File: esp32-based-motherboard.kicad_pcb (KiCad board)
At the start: 2 copper layers, 4 parts, among them J1 HR911105A, U1 ESP32-P4_MODULE, U2 LAN8720A, U3 ADM3053

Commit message: Finalized schematics V1
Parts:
- added C1: 470UF, Capacitor_THT:CP_Radial_D6.3mm_P2.50mm, F.Cu at (150.7, 64.6)
- added C10: 0.1uF, Capacitor_SMD:C_0603_1608Metric, F.Cu at (123.8, 72.0)
- added C11: 10uF, Capacitor_SMD:C_0603_1608Metric, F.Cu at (169.9, 105.5)
- added C12: 0.1uF, Capacitor_SMD:C_0603_1608Metric, F.Cu at (169.9, 108.0)
- added C13: 0.1uF, Capacitor_SMD:C_0603_1608Metric, F.Cu at (169.9, 110.5)
- added C14: 0.1uF, Capacitor_SMD:C_0603_1608Metric, F.Cu at (169.9, 113.0)
- added C15: 470pF, Capacitor_SMD:C_0603_1608Metric, F.Cu at (169.9, 115.6)
- added C16: 1uF, Capacitor_SMD:C_0603_1608Metric, F.Cu at (173.9, 105.5)
- added C17: 12pF, Capacitor_SMD:C_0603_1608Metric, F.Cu at (173.9, 108.0)
- added C18: 12pF, Capacitor_SMD:C_0603_1608Metric, F.Cu at (173.9, 110.5)
- added C19: 0.1uF, Capacitor_SMD:C_0603_1608Metric, F.Cu at (123.8, 74.5)
- added C2: 47UF, Capacitor_THT:CP_Radial_D6.3mm_P2.50mm, F.Cu at (150.7, 72.4)
- added C20: 10uF, Capacitor_SMD:C_0603_1608Metric, F.Cu at (123.8, 77.0)
- added C21: 0.01uF, Capacitor_SMD:C_0603_1608Metric, F.Cu at (127.8, 61.9)
- added C22: 0.1uF, Capacitor_SMD:C_0603_1608Metric, F.Cu at (127.8, 64.4)
- added C23: 10uF, Capacitor_SMD:C_0603_1608Metric, F.Cu at (127.8, 66.9)
- added C24: 10nF, Capacitor_SMD:C_0603_1608Metric, F.Cu at (127.8, 69.4)
- added C25: 100nF, Capacitor_SMD:C_0603_1608Metric, F.Cu at (127.8, 72.0)
- added C26: 0.1uF, Capacitor_SMD:C_0603_1608Metric, F.Cu at (127.8, 74.5)
- added C28: 10uF, Capacitor_SMD:C_0603_1608Metric, F.Cu at (127.8, 77.0)
- added C29: 0.1uF, Capacitor_SMD:C_0603_1608Metric, F.Cu at (131.8, 61.9)
- added C3: 10uF, Capacitor_SMD:C_0603_1608Metric, F.Cu at (167.2, 86.6)
- added C30: 0.1uF, Capacitor_SMD:C_0603_1608Metric, F.Cu at (131.8, 64.4)
- added C31: 10uF, Capacitor_SMD:C_0603_1608Metric, F.Cu at (131.8, 66.9)
- added C4: 470UF, Capacitor_THT:CP_Radial_D6.3mm_P2.50mm, F.Cu at (150.7, 80.3)
- added C5: 47UF, Capacitor_THT:CP_Radial_D6.3mm_P2.50mm, F.Cu at (150.7, 88.1)
- added C6: 10uF, Capacitor_SMD:C_0603_1608Metric, F.Cu at (123.8, 61.9)
- added C7: 0.1uF, Capacitor_SMD:C_0603_1608Metric, F.Cu at (123.8, 64.4)
- added C8: 0.1uF, Capacitor_SMD:C_0603_1608Metric, F.Cu at (123.8, 66.9)
- added C9: 10uF, Capacitor_SMD:C_0603_1608Metric, F.Cu at (123.8, 69.4)
- added D1: SS56, Diode_SMD:D_SMB, F.Cu at (173.4, 96.5)
- added D10: SD05C-01F, Diode_SMD:D_SOD-323, F.Cu at (113.7, 113.5)
- added D11: SD05C-01F, Diode_SMD:D_SOD-323, F.Cu at (118.0, 104.7)
- added D12: SD05C-01F, Diode_SMD:D_SOD-323, F.Cu at (118.0, 107.6)
- added D13: SD05C-01F, Diode_SMD:D_SOD-323, F.Cu at (118.0, 110.6)
- added D14: SD05C-01F, Diode_SMD:D_SOD-323, F.Cu at (118.0, 113.5)
- added D15: SD05C-01F, Diode_SMD:D_SOD-323, F.Cu at (122.3, 104.7)
- added D16: LED, LED_SMD:LED_0603_1608Metric, F.Cu at (138.1, 107.8)
- added D17: LED, LED_SMD:LED_0603_1608Metric, F.Cu at (138.1, 110.4)
- added D18: SD05C-01F, Diode_SMD:D_SOD-323, F.Cu at (122.3, 107.6)
- added D19: SD05C-01F, Diode_SMD:D_SOD-323, F.Cu at (122.3, 110.6)
- added D2: 1N5822, Diode_SMD:D_SMA, F.Cu at (183.1, 87.6)
- added D20: SD05C-01F, Diode_SMD:D_SOD-323, F.Cu at (122.3, 113.5)
- added D3: LED, LED_SMD:LED_0603_1608Metric, F.Cu at (149.9, 93.4)
- added D4: 1N5822, Diode_SMD:D_SMA, F.Cu at (183.1, 92.2)
- added D5: LED, LED_SMD:LED_0603_1608Metric, F.Cu at (149.9, 95.9)
- added D6: LED, LED_SMD:LED_0603_1608Metric, F.Cu at (149.9, 98.5)
- added D7: ESD7951ST5G, Diode_SMD:D_SOD-323, F.Cu at (113.7, 104.7)
- added D8: ESD7951ST5G, Diode_SMD:D_SOD-323, F.Cu at (113.7, 107.6)
- added D9: SD05C-01F, Diode_SMD:D_SOD-323, F.Cu at (113.7, 110.6)
- added F1: Fuse, Fuse:Fuseholder_Littelfuse_Nano2_157x, F.Cu at (183.5, 97.1)
- added FB1: FerriteBead, Inductor_SMD:L_0603_1608Metric, F.Cu at (131.8, 69.4)
- added FB2: FerriteBead, Inductor_SMD:L_0603_1608Metric, F.Cu at (131.8, 72.0)
- added J2: RJ45_Hanrun_HR911105A_Horizontal, Connector_RJ:RJ45_Hanrun_HR911105A_Horizontal, F.Cu at (153.5, 109.3)
- added J3: USB_C_Receptacle_USB2.0_16P, Connector_USB:USB_C_Receptacle_Palconn_UTC16-G, F.Cu at (130.2, 92.8)
- added J4: USB_A, Connector_USB:USB_A_Molex_67643_Horizontal, F.Cu at (98.9, 92.0)
- added J5: USB_C_Receptacle_USB2.0_16P, Connector_USB:USB_C_Receptacle_Palconn_UTC16-G, F.Cu at (130.2, 102.8)
- added J6: USB_C_Receptacle_USB2.0_16P, Connector_USB:USB_C_Receptacle_Palconn_UTC16-G, F.Cu at (130.2, 112.8)
- added J7: Conn_01x03_Pin, Connector_JST:JST_PH_B3B-PH-K_1x03_P2.00mm_Vertical, F.Cu at (96.3, 108.7)
- added J8: Conn_01x03_Pin, Connector_JST:JST_PH_B3B-PH-K_1x03_P2.00mm_Vertical, F.Cu at (96.3, 115.3)
- added L1: 47uH, Inductor_SMD:L_Wuerth_HCI-7030, F.Cu at (160.5, 89.6)
- added L2: 47uH, Inductor_SMD:L_Wuerth_HCI-7030, F.Cu at (160.5, 98.0)
- added R1: 2k, Resistor_SMD:R_0603_1608Metric, F.Cu at (167.2, 89.1)
- added R10: 10k, Resistor_SMD:R_0603_1608Metric, F.Cu at (135.8, 72.0)
- added R11: 10k, Resistor_SMD:R_0603_1608Metric, F.Cu at (135.8, 74.5)
- added R12: 5.1k, Resistor_SMD:R_0603_1608Metric, F.Cu at (135.8, 77.0)
- added R13: 10k, Resistor_SMD:R_0603_1608Metric, F.Cu at (139.9, 61.9)
- added R14: 5.1k, Resistor_SMD:R_0603_1608Metric, F.Cu at (139.9, 64.4)
- added R15: 10k, Resistor_SMD:R_0603_1608Metric, F.Cu at (139.9, 66.9)
- added R17: 5.1k, Resistor_SMD:R_0603_1608Metric, F.Cu at (139.9, 69.4)
- added R18: 5.1k, Resistor_SMD:R_0603_1608Metric, F.Cu at (139.9, 72.0)
- added R19: 47k, Resistor_SMD:R_0603_1608Metric, F.Cu at (139.9, 74.5)
- added R2: 1k, Resistor_SMD:R_0603_1608Metric, F.Cu at (167.2, 91.6)
- added R20: 1k, Resistor_SMD:R_0603_1608Metric, F.Cu at (139.9, 77.0)
- added R21: 10k, Resistor_SMD:R_0603_1608Metric, F.Cu at (143.9, 61.9)
- added R22: 500, Resistor_SMD:R_0603_1608Metric, F.Cu at (173.9, 113.0)
- added R23: 1k, Resistor_SMD:R_0603_1608Metric, F.Cu at (143.9, 64.4)
- added R24: 0, Resistor_SMD:R_0603_1608Metric, F.Cu at (143.9, 66.9)
- added R25: 120, Resistor_SMD:R_0603_1608Metric, F.Cu at (143.9, 69.4)
- added R26: 10k, Resistor_SMD:R_0603_1608Metric, F.Cu at (173.9, 115.6)
- added R27: 10k, Resistor_SMD:R_0603_1608Metric, F.Cu at (177.9, 105.5)
- added R28: 12.1k (1%), Resistor_SMD:R_0603_1608Metric, F.Cu at (177.9, 108.0)
- added R29: 10k, Resistor_SMD:R_0603_1608Metric, F.Cu at (143.9, 72.0)
- added R3: 500, Resistor_SMD:R_0603_1608Metric, F.Cu at (167.2, 94.1)
- added R30: 500, Resistor_SMD:R_0603_1608Metric, F.Cu at (177.9, 110.5)
- added R31: 1k, Resistor_SMD:R_0603_1608Metric, F.Cu at (143.9, 74.5)
- added R4: 0, Resistor_SMD:R_0603_1608Metric, F.Cu at (131.8, 74.5)
- added R5: 0, Resistor_SMD:R_0603_1608Metric, F.Cu at (131.8, 77.0)
- added R6: 0, Resistor_SMD:R_0603_1608Metric, F.Cu at (135.8, 61.9)
- added R7: 0, Resistor_SMD:R_0603_1608Metric, F.Cu at (135.8, 64.4)
- added R8: 5.1k, Resistor_SMD:R_0603_1608Metric, F.Cu at (135.8, 66.9)
- added R9: 5.1k, Resistor_SMD:R_0603_1608Metric, F.Cu at (135.8, 69.4)
- added SW1: SW_Push, Button_Switch_SMD:SW_Push_SPST_NO_Alps_SKRK, F.Cu at (139.3, 90.9)
- added SW2: SW_Push, Button_Switch_SMD:SW_Push_SPST_NO_Alps_SKRK, F.Cu at (139.3, 95.4)
- added SW3: SW_Push, Button_Switch_SMD:SW_Push_SPST_NO_Alps_SKRK, F.Cu at (139.3, 99.8)
- added SW4: SW_Push, Button_Switch_SMD:SW_Push_SPST_NO_Alps_SKRK, F.Cu at (139.3, 104.3)
- added SW5: SW_SPST, Custom_Footprint:DSIC01LHGET_C54957, F.Cu at (117.2, 115.7)
- added U12: CP2102N-Axx-xQFN24, Package_DFN_QFN:QFN-24-1EP_4x4mm_P0.5mm_EP2.6x2.6mm, F.Cu at (106.8, 109.1)
- added U5: ESP32-P4_MODULE, Custom_Footprint:ESP32-P4_MODULE, F.Cu at (107.8, 74.7)
- added U6: ADM3053, Package_SO:SOIC-20W_7.5x12.8mm_P1.27mm, F.Cu at (118.0, 96.0)
- added U7: LAN8720A, Package_DFN_QFN:VQFN-24-1EP_4x4mm_P0.5mm_EP2.5x2.5mm_ThermalVias, F.Cu at (171.4, 120.0)
- added Y1: 25MHz, Crystal:Crystal_SMD_3225-4Pin_3.2x2.5mm, F.Cu at (177.2, 119.1)
- J1: value HR911105A -> XT30PW-M; footprint Connector_RJ:HANRUN_HR911105A -> Custom_Footprint:AMASS_XT30PW-M
- U1: value ESP32-P4_MODULE -> LM2596S-12; footprint ESP32-P4:XCVR_ESP32-P4_MODULE -> Package_TO_SOT_SMD:TO-263-5_TabPin3
- U2: value LAN8720A -> LM2596S-5; footprint Package_DFN_QFN:QFN-24-1EP_4x4mm_P0.5mm_EP2.6x2.6mm -> Package_TO_SOT_SMD:TO-263-5_TabPin3
- U3: value ADM3053 -> AMS1117-3.3; footprint Package_SO:SOIC-20W_7.5x12.8mm_P1.27mm -> Package_TO_SOT_SMD:SOT-223-3_TabPin2
- moved U1 59.2 mm to (166.6, 66.8)
- moved U3 52.9 mm to (174.1, 89.6)
- moved U2 36.8 mm to (166.6, 79.2)
- moved J1 36.4 mm to (181.0, 64.4)
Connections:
- U1 pad 1: GND -> /power_system/Vcc
- U1 pad 2: unconnected-(U1-LNA_OUT-Pad2) -> Net-(D2-K)
- U1 pad 4: unconnected-(U1-C6_U0RXD-Pad4) -> +12V
- U1 pad 5: unconnected-(U1-C6_U0TXD-Pad5) -> GND
- U2 pad 1: unconnected-(U2-VDD2A-Pad1) -> /power_system/Vcc
- U2 pad 3: unconnected-(U2-LED1/REGOFF-Pad3) -> GND
- U2 pad 4: unconnected-(U2-XTAL2-Pad4) -> +5V
- U2 pad 5: unconnected-(U2-XTAL1/CLKIN-Pad5) -> GND
- U3 pad 1: unconnected-(U3-GND1-Pad1) -> GND
- U3 pad 2: unconnected-(U3-NC-Pad2) -> +3.3V
- U3 pad 3: unconnected-(U3-GND1-Pad3) -> +5V

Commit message: Updated Footprint
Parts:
- removed R31: 1k, Resistor_SMD:R_0603_1608Metric
- removed U12: CP2102N-Axx-xQFN24, Package_DFN_QFN:QFN-24-1EP_4x4mm_P0.5mm_EP2.6x2.6mm
- added C27: 47UF, Capacitor_THT:CP_Radial_D6.3mm_P2.50mm, F.Cu at (43.1, 105.7)
- added H1: MountingHole_Pad, MountingHole:MountingHole_3.2mm_M3_Pad, F.Cu at (28.1, 132.8)
- added H2: MountingHole_Pad, MountingHole:MountingHole_3.2mm_M3_Pad, F.Cu at (102.3, 133.3)
- added H3: MountingHole_Pad, MountingHole:MountingHole_3.2mm_M3_Pad, F.Cu at (26.5, 79.2)
- added H4: MountingHole_Pad, MountingHole:MountingHole_3.2mm_M3_Pad, F.Cu at (103.6, 79.2)
- added J10: Conn_01x02_Pin, Connector_AMASS:AMASS_XT30PW-F_1x02_P2.50mm_Horizontal, F.Cu at (92.9, 114.2)
- added J11: Conn_01x02_Pin, Connector_AMASS:AMASS_XT30PW-F_1x02_P2.50mm_Horizontal, F.Cu at (92.9, 99.7)
- added J9: Conn_01x02_Pin, Connector_AMASS:AMASS_XT30PW-F_1x02_P2.50mm_Horizontal, F.Cu at (37.1, 107.9)
- added R16: 10k, Resistor_SMD:R_0603_1608Metric, F.Cu at (52.5, 76.0)
- added U4: LAN8720A, Package_DFN_QFN:VQFN-24-1EP_4x4mm_P0.5mm_EP2.5x2.5mm_ThermalVias, F.Cu at (54.1, 95.1)
- C1: value 470UF -> 10uF; footprint Capacitor_THT:CP_Radial_D6.3mm_P2.50mm -> Capacitor_SMD:C_0603_1608Metric
- C10: value 0.1uF -> 0.01uF
- C11, C23, C6: value 10uF -> 0.1uF
- C13, C30: value 0.1uF -> 10uF
- C15: value 470pF -> 10uF
- C16: value 1uF -> 10nF
- C17: value 12pF -> 100nF
- C19: value 0.1uF -> 12pF
- C2: value 47UF -> 0.1uF; footprint Capacitor_THT:CP_Radial_D6.3mm_P2.50mm -> Capacitor_SMD:C_0603_1608Metric
- C21: value 0.01uF -> 0.1uF
- C24: value 10nF -> 470pF
- C25: value 100nF -> 1uF
- C26: value 0.1uF -> 470UF; footprint Capacitor_SMD:C_0603_1608Metric -> Capacitor_THT:CP_Radial_D6.3mm_P2.50mm
- C28: value 10uF -> 470UF; footprint Capacitor_SMD:C_0603_1608Metric -> Capacitor_THT:CP_Radial_D6.3mm_P2.50mm
- C29: value 0.1uF -> 47UF; footprint Capacitor_SMD:C_0603_1608Metric -> Capacitor_THT:CP_Radial_D6.3mm_P2.50mm
- C4: value 470UF -> 0.1uF; footprint Capacitor_THT:CP_Radial_D6.3mm_P2.50mm -> Capacitor_SMD:C_0603_1608Metric
- C5: value 47UF -> 10uF; footprint Capacitor_THT:CP_Radial_D6.3mm_P2.50mm -> Capacitor_SMD:C_0603_1608Metric
- D1: value SS56 -> SD05C-01F; footprint Diode_SMD:D_SMB -> Diode_SMD:D_SOD-323
- D13, D14, D19, D20: value SD05C-01F -> LED; footprint Diode_SMD:D_SOD-323 -> LED_SMD:LED_0603_1608Metric
- D15: value SD05C-01F -> SS56; footprint Diode_SMD:D_SOD-323 -> Diode_SMD:D_SMB
- D16: value LED -> 1N5822; footprint LED_SMD:LED_0603_1608Metric -> Diode_SMD:D_SMA
- D18: value SD05C-01F -> 1N5822; footprint Diode_SMD:D_SOD-323 -> Diode_SMD:D_SMA
- D2: value 1N5822 -> SD05C-01F; footprint Diode_SMD:D_SMA -> Diode_SMD:D_SOD-323
- D3, D5: value LED -> SD05C-01F; footprint LED_SMD:LED_0603_1608Metric -> Diode_SMD:D_SOD-323
- D4: value 1N5822 -> ESD7951ST5G; footprint Diode_SMD:D_SMA -> Diode_SMD:D_SOD-323
- D6: value LED -> ESD7951ST5G; footprint LED_SMD:LED_0603_1608Metric -> Diode_SMD:D_SOD-323
- D7, D8: value ESD7951ST5G -> SD05C-01F
- F1: footprint Fuse:Fuseholder_Littelfuse_Nano2_157x -> Fuse:Fuseholder_Cylinder-5x20mm_Schurter_0031_8201_Horizontal_Open
- J1: value XT30PW-M -> USB_A; footprint Custom_Footprint:AMASS_XT30PW-M -> Connector_USB:USB_A_Molex_67643_Horizontal
- J2: value RJ45_Hanrun_HR911105A_Horizontal -> USB_C_Receptacle_USB2.0_16P; footprint Connector_RJ:RJ45_Hanrun_HR911105A_Horizontal -> Connector_USB:USB_C_Receptacle_Palconn_UTC16-G
- J4: value USB_A -> USB_C_Receptacle_USB2.0_16P; footprint Connector_USB:USB_A_Molex_67643_Horizontal -> Connector_USB:USB_C_Receptacle_Palconn_UTC16-G
- J5, J6: value USB_C_Receptacle_USB2.0_16P -> Conn_01x03_Pin; footprint Connector_USB:USB_C_Receptacle_Palconn_UTC16-G -> Connector_JST:JST_PH_B3B-PH-K_1x03_P2.00mm_Vertical
- J7: value Conn_01x03_Pin -> RJ45_Hanrun_HR911105A_Horizontal; footprint Connector_JST:JST_PH_B3B-PH-K_1x03_P2.00mm_Vertical -> Connector_RJ:RJ45_Hanrun_HR911105A_Horizontal
- J8: value Conn_01x03_Pin -> Conn_01x02_Pin; footprint Connector_JST:JST_PH_B3B-PH-K_1x03_P2.00mm_Vertical -> Connector_AMASS:AMASS_XT30PW-M_1x02_P2.50mm_Horizontal
- R1: value 2k -> 5.1k
- R10: value 10k -> 5.1k
- R12: value 5.1k -> 47k
- R13, R15, R29: value 10k -> 1k
- R14: value 5.1k -> 1k
- R17, R18: value 5.1k -> 10k
- R19: value 47k -> 10k
- R2: value 1k -> 5.1k
- R20: value 1k -> 0
- R22: value 500 -> 120
- R23: value 1k -> 10k
- R24: value 0 -> 12.1k (1%)
- R25: value 120 -> 10k
- R26, R27: value 10k -> 500
- R28: value 12.1k (1%) -> 2k
- R3: value 500 -> 5.1k
- R4: value 0 -> 5.1k
- R8: value 5.1k -> 0
- U1: value LM2596S-12 -> ESP32-P4_MODULE; footprint Package_TO_SOT_SMD:TO-263-5_TabPin3 -> Custom_Footprint:ESP32-P4_MODULE
- U2: value LM2596S-5 -> CP2102N-Axx-xQFN24; footprint Package_TO_SOT_SMD:TO-263-5_TabPin3 -> Package_DFN_QFN:QFN-24-1EP_4x4mm_P0.5mm_EP2.6x2.6mm
- U3: value AMS1117-3.3 -> ADM3053; footprint Package_TO_SOT_SMD:SOT-223-3_TabPin2 -> Package_SO:SOIC-20W_7.5x12.8mm_P1.27mm
- U5: value ESP32-P4_MODULE -> LM2596S-12; footprint Custom_Footprint:ESP32-P4_MODULE -> Package_TO_SOT_SMD:TO-263-5_TabPin3
- U6: value ADM3053 -> LM2596S-5; footprint Package_SO:SOIC-20W_7.5x12.8mm_P1.27mm -> Package_TO_SOT_SMD:TO-263-5_TabPin3
- U7: value LAN8720A -> AMS1117-3.3; footprint Package_DFN_QFN:VQFN-24-1EP_4x4mm_P0.5mm_EP2.5x2.5mm_ThermalVias -> Package_TO_SOT_SMD:SOT-223-3_TabPin2
- moved F1 146.3 mm to (41.5, 132.5)
- moved R26 144.7 mm to (41.8, 56.6), turned to 90 degrees
- moved R27 143.6 mm to (41.8, 59.9), turned to -90 degrees
- moved R28 133.5 mm to (44.5, 111.8), turned to 180 degrees
- moved Y1 131.1 mm to (48.3, 95.0)
- moved U2 128.6 mm to (38.4, 88.7)
- moved D2 128.0 mm to (56.1, 72.5)
- moved C18 126.3 mm to (48.3, 97.6)
- moved R3 117.4 mm to (53.1, 66.6)
- moved C3 117.0 mm to (51.3, 102.4)
- moved J1 113.4 mm to (67.6, 68.3), turned to 180 degrees
- moved C5 111.7 mm to (39.3, 97.3), turned to 180 degrees
- moved D1 111.7 mm to (64.4, 72.3), turned to 180 degrees
- moved D4 110.1 mm to (75.4, 69.2)
- moved D5 107.6 mm to (46.4, 66.5)
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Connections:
- C1 pad 1: /power_system/Vcc -> +5V
- C12 pad 1: GND -> +5V
- C12 pad 2: +3.3V -> GND
- C13 pad 1: GND -> +5V
- C13 pad 2: +3.3V -> GND
- C14 pad 1: GND -> Net-(C14-Pad1)
- C14 pad 2: +3.3V -> Net-(U3-VISOOUT)
- C15 pad 1: Net-(C15-Pad1) -> GNDREF
- C15 pad 2: GND -> Net-(U3-VISOIN)
- C16 pad 1: Net-(C15-Pad1) -> GNDREF
- C16 pad 2: GND -> Net-(U3-VISOIN)
- C17 pad 1: GND -> GNDREF
- C17 pad 2: XTAL1 -> Net-(U3-VISOIN)
- C18 pad 2: XTAL2 -> XTAL1
- C19 pad 2: +3.3V -> XTAL2
- C2 pad 1: +12V -> +5V
- C20 pad 1: +5V -> GND
- C20 pad 2: GND -> +3.3V
- C22 pad 1: Net-(C22-Pad1) -> GND
- C22 pad 2: Net-(U6-VISOOUT) -> +3.3V
- C23 pad 1: GNDREF -> GND
- C23 pad 2: Net-(U6-VISOIN) -> +3.3V
- C24 pad 1: GNDREF -> Net-(U4-VDDCR)
- C24 pad 2: Net-(U6-VISOIN) -> GND
- C25 pad 1: GNDREF -> Net-(U4-VDDCR)
- C25 pad 2: Net-(U6-VISOIN) -> GND
- C26 pad 1: +5V -> /power_system/Vcc
- C28 pad 1: GND -> /power_system/Vcc
- C28 pad 2: +5V -> GND
- C29 pad 1: GND -> +5V
- C29 pad 2: +5V -> GND
- C3 pad 1: +3.3V -> GND
- C3 pad 2: GND -> +3.3V
- C30 pad 1: GND -> +3.3V
- C30 pad 2: +3.3V -> GND
- C31 pad 1: GND -> +5V
- C31 pad 2: +3.3V -> GND
- C4 pad 1: /power_system/Vcc -> GND
- C4 pad 2: GND -> +3.3V
- C5 pad 1: +5V -> GND
- C5 pad 2: GND -> +5V
- C6 pad 1: +5V -> GND
- C6 pad 2: GND -> +5V
- C7 pad 1: +5V -> GND
- C7 pad 2: GND -> +3.3V
- D1 pad 1: /power_system/Vcc -> GND
- D1 pad 2: GND -> /USB_A_DM
- D10 pad 2: /USB_A_DM -> D+
- D11 pad 2: /USB_A_DP -> D-
- D13 pad 2: USB1P1_P -> Net-(D13-A)
- D14 pad 2: USB1P1_N -> Net-(D14-A)
- D15 pad 1: GND -> /power_system/Vcc
- D15 pad 2: +5V -> GND
- D16 pad 1: GND -> Net-(D16-K)
- D16 pad 2: Net-(D16-A) -> GND
- D18 pad 1: GND -> Net-(D18-K)
- D18 pad 2: D+ -> GND
- D19 pad 2: D- -> Net-(D19-A)
- D2 pad 1: Net-(D2-K) -> GND
- D2 pad 2: GND -> /USB_A_DP
- D20 pad 2: +5V -> Net-(D20-A)
- D3 pad 2: Net-(D3-A) -> +5V
- D4 pad 1: unconnected-(D4-K-Pad1) -> GND
- D4 pad 2: GND -> /USB_C_DP
- D5 pad 2: Net-(D5-A) -> USB1P1_P
- D6 pad 2: Net-(D6-A) -> /USB_C_DM
- D7 pad 2: /USB_C_DP -> USB1P1_N
- D8 pad 2: /USB_C_DM -> +5V
- F1 pad 1: unconnected-(J1-PadP) -> Net-(J8-Pin_2)
- FB1 pad 1: Net-(C22-Pad1) -> Net-(C14-Pad1)
- FB2 pad 1: Net-(U6-VISOIN) -> Net-(U3-VISOIN)
- FB2 pad 2: Net-(U6-VISOOUT) -> Net-(U3-VISOOUT)
- J3 pad A6: /USB_C_DP -> USB1P1_P
- J3 pad A7: /USB_C_DM -> USB1P1_N
- J3 pad B6: /USB_C_DP -> USB1P1_P
- J3 pad B7: /USB_C_DM -> USB1P1_N
- J7 pad 1: CAN_H -> TD+
- J7 pad 2: CAN_L -> TD-
- J7 pad 3: GNDREF -> RD+
- J8 pad 1: CAN_H -> GND
- J8 pad 2: CAN_L -> Net-(J8-Pin_2)
- L1 pad 1: Net-(D2-K) -> Net-(D16-K)
- L2 pad 1: unconnected-(D4-K-Pad1) -> Net-(D18-K)
- R1 pad 1: +12V -> Net-(J2-CC1)
- R1 pad 2: Net-(D3-A) -> GND
- R10 pad 1: +3.3V -> Net-(J4-CC2)
- R10 pad 2: BOOT -> GND
- R11 pad 1: +3.3V -> Net-(U2-VBUS)
- R11 pad 2: C6_BOOT -> +5V
- R12 pad 1: Net-(J5-CC1) -> GND
- R12 pad 2: GND -> Net-(U2-VBUS)
- R13 pad 1: +3.3V -> Net-(U2-~{RST})
- R13 pad 2: BOOT_EN -> +3.3V
- R14 pad 1: Net-(J5-CC2) -> Net-(D13-A)
- R14 pad 2: GND -> Net-(U2-~{TXT}/GPIO.0)
- R15 pad 1: +3.3V -> Net-(D14-A)
- R15 pad 2: C6_BOOT_EN -> Net-(U2-~{RXT}/GPIO.1)
- R17 pad 1: Net-(J6-CC1) -> +3.3V
- R17 pad 2: GND -> BOOT
- R18 pad 1: Net-(J6-CC2) -> +3.3V
- R18 pad 2: GND -> C6_BOOT
- R19 pad 1: GND -> +3.3V
- R19 pad 2: Net-(U12-VBUS) -> BOOT_EN
- R2 pad 1: +5V -> Net-(J2-CC2)
- R2 pad 2: Net-(D5-A) -> GND
- R20 pad 1: Net-(U12-~{RST}) -> GNDREF
- R20 pad 2: +3.3V -> Net-(U3-RS)
- R21 pad 1: Net-(U12-VBUS) -> +3.3V
- R21 pad 2: +5V -> C6_BOOT_EN
- R22 pad 1: GND -> Net-(SW5-A)
- R22 pad 2: unconnected-(R22-Pad2) -> CAN_H
- R23 pad 1: Net-(D16-A) -> PHY_LED1
- R23 pad 2: Net-(U12-~{TXT}/GPIO.0) -> GND
- R24 pad 1: GNDREF -> Net-(U4-RBIAS)
- R24 pad 2: Net-(U6-RS) -> GND
- R25 pad 1: Net-(SW5-A) -> PHY_LED2
- R25 pad 2: CAN_H -> GND
- R26 pad 1: PHY_LED1 -> GND
- R26 pad 2: GND -> Net-(J7-Pad11)
- R27 pad 1: PHY_LED2 -> GND
- R27 pad 2: GND -> Net-(J7-Pad10)
- R28 pad 1: unconnected-(R28-Pad1) -> +12V
- R28 pad 2: GND -> Net-(D17-A)
- R29 pad 1: +3.3V -> +5V
- R29 pad 2: EN -> Net-(D19-A)
- R3 pad 1: +3.3V -> Net-(J3-CC1)
- R3 pad 2: Net-(D6-A) -> GND
- R30 pad 1: GND -> +3.3V
- R30 pad 2: unconnected-(R30-Pad2) -> Net-(D20-A)
- R4 pad 1: /USB_A_DP -> Net-(J3-CC2)
- R4 pad 2: USB_DP -> GND
- R5 pad 1: /USB_A_DM -> /USB_A_DP
- R5 pad 2: USB_DM -> USB_DP
- R6 pad 1: /USB_C_DM -> /USB_A_DM
- R7 pad 1: /USB_C_DP -> /USB_C_DM
- R7 pad 2: USB_DP -> USB_DM
- R8 pad 1: Net-(J3-CC1) -> /USB_C_DP
- R8 pad 2: GND -> USB_DP
- R9 pad 1: Net-(J3-CC2) -> Net-(J4-CC1)
- U1 pad 1: /power_system/Vcc -> GND
- U1 pad 2: Net-(D2-K) -> unconnected-(U1-LNA_OUT-Pad2)
- U1 pad 4: +12V -> C6_UART_RX
- U1 pad 5: GND -> C6_UART_TX
- U2 pad 1: /power_system/Vcc -> unconnected-(U2-~{RI}/CLK-Pad1)
- U2 pad 2: unconnected-(D4-K-Pad1) -> GND
- U2 pad 3: GND -> D+
- U2 pad 4: +5V -> D-
- U2 pad 5: GND -> +3.3V
- U3 pad 2: +3.3V -> unconnected-(U3-NC-Pad2)
- U3 pad 3: +5V -> GND
- U5 pad 1: GND -> /power_system/Vcc
- U5 pad 2: unconnected-(U5-LNA_OUT-Pad2) -> Net-(D16-K)
- U5 pad 4: C6_UART_RX -> +12V
- U5 pad 5: C6_UART_TX -> GND
- U6 pad 1: GND -> /power_system/Vcc
- U6 pad 2: unconnected-(U6-NC-Pad2) -> Net-(D18-K)
- U6 pad 4: CAN_RX -> +5V
- U6 pad 5: CAN_TX -> GND
- U7 pad 1: +3.3V -> GND
- U7 pad 2: PHY_LED2 -> +3.3V
- U7 pad 3: PHY_LED1 -> +5V
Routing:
- net Net-(U2-VBUS): track 0.00 -> 3.85 mm
- added copper zone on In1.Cu, net GND
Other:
- board outline added: 85.2 x 83.8 mm
- copper layers 2 -> 4

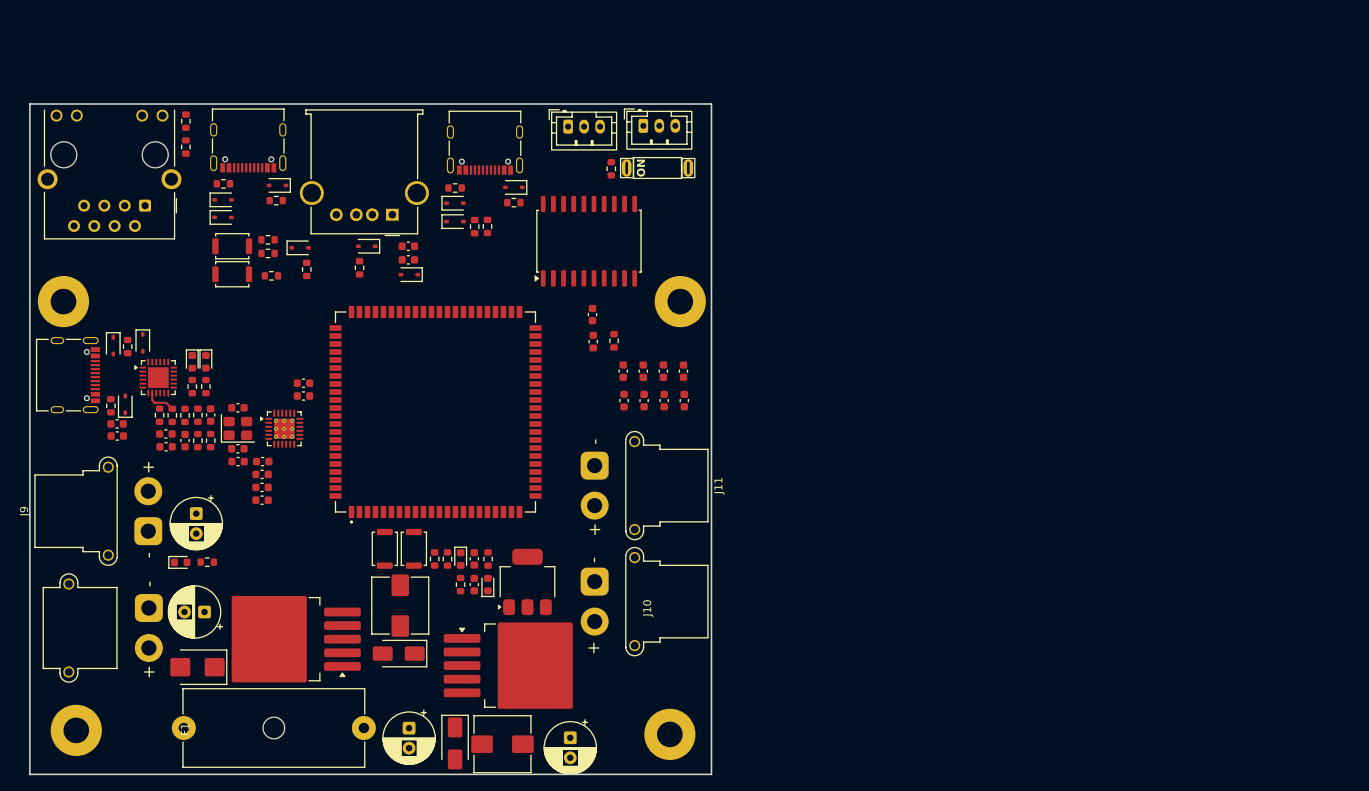
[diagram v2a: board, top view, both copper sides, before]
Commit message: Track and Vias added
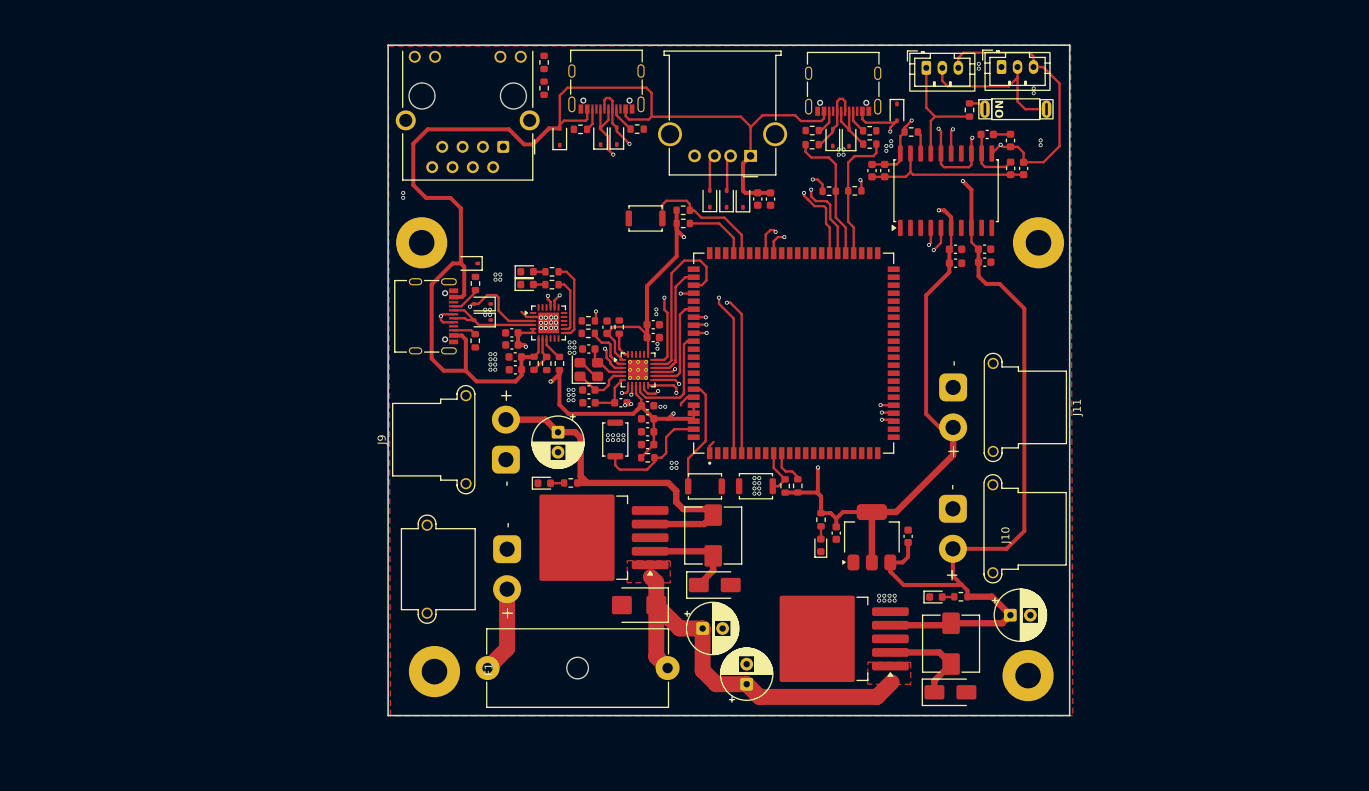
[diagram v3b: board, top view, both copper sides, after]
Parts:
- moved R5 66.0 mm to (122.2, 65.4), turned to 0 degrees
- moved R6 62.6 mm to (125.4, 65.4), turned to 180 degrees
- moved R29 62.6 mm to (138.7, 116.1), turned to 180 degrees
- moved C26 62.3 mm to (106.4, 120.1), turned to 0 degrees
- moved D18 62.2 mm to (137.4, 128.0), turned to 0 degrees
- moved D19 59.6 mm to (135.6, 116.1), turned to 0 degrees
- moved FB1 58.2 mm to (144.9, 59.1)
- moved C22 58.0 mm to (99.5, 92.2), turned to 180 degrees
- moved L2 57.5 mm to (137.4, 122.0), turned to 90 degrees
- moved C29 57.1 mm to (144.9, 118.4), turned to 0 degrees
- moved FB2 56.5 mm to (144.9, 62.5), turned to 90 degrees
- moved D15 55.7 mm to (98.5, 117.1)
- moved C17 55.6 mm to (146.5, 62.6)
- moved C31 54.6 mm to (132.1, 108.5)
- moved C14 54.2 mm to (142.0, 58.3), turned to 180 degrees
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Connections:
- R23 pad 1: PHY_LED1 -> PHY_LED2
- R25 pad 1: PHY_LED2 -> PHY_LED1
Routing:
- net +5V: track 0.00 -> 289.9 mm, vias 0 -> 2
- net +3.3V: track 0.00 -> 212.4 mm, vias 0 -> 6
- net GNDREF: track 0.00 -> 65.2 mm, vias 0 -> 4
- net /power_system/Vcc: track 0.00 -> 50.3 mm
- net USB1P1_N: track 0.00 -> 45.0 mm, vias 0 -> 2
- net +12V: track 0.00 -> 44.8 mm
- net USB1P1_P: track 0.00 -> 44.7 mm, vias 0 -> 2
- net C6_UART_RX: track 0.00 -> 44.1 mm, vias 0 -> 2
- net C6_UART_TX: track 0.00 -> 42.9 mm, vias 0 -> 2
- net CAN_L: track 0.00 -> 36.8 mm, vias 0 -> 1
- net PHY_MDC: track 0.00 -> 36.7 mm, vias 0 -> 2
- net PHY_MDIO: track 0.00 -> 35.4 mm, vias 0 -> 2
- net PHY_Reset: track 0.00 -> 35.1 mm, vias 0 -> 2
- net CAN_H: track 0.00 -> 28.9 mm
- net CAN_TX: track 0.00 -> 28.4 mm, vias 0 -> 2
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- added copper zone on F.Cu, net /power_system/Vcc
- added copper zone on F.Cu, net GND

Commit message: updated
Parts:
- moved D9 9.95 mm to (98.4, 57.3), turned to 180 degrees
- moved D3 5.84 mm to (108.3, 61.4)
- moved D1 5.84 mm to (106.3, 61.4)
- moved D2 5.84 mm to (104.2, 61.4)
- moved C1 5.84 mm to (111.8, 61.4)
- moved C2 5.84 mm to (110.2, 61.4)
- moved R24 4.54 mm to (92.1, 80.0), turned to 180 degrees
- moved J1 4.33 mm to (112.5, 56.7)
- moved D7 3.80 mm to (95.4, 62.3), turned to 180 degrees
- moved R17 1.94 mm to (104.5, 69.7)
- moved SW2 1.94 mm to (99.8, 70.7)
- moved R19 1.94 mm to (104.5, 71.3)
- moved D11 1.93 mm to (79.8, 83.2), turned to 90 degrees
- moved D5 1.62 mm to (92.4, 59.5), turned to 0 degrees
- moved R3 1.50 mm to (98.3, 59.1)
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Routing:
- net +5V: track 289.9 -> 169.5 mm
- net USB_DP: track 16.9 -> 0.00 mm
- net BOOT: track 16.3 -> 0.00 mm
- net +3.3V: track 212.4 -> 200.1 mm, vias 6 -> 7
- net RMII_RXD0: track 26.0 -> 14.7 mm
- net BOOT_EN: track 8.13 -> 0.00 mm
- net USB_DM: track 16.7 -> 8.67 mm
- net RMII_TXD0: track 22.2 -> 14.2 mm
- net D+: track 18.8 -> 13.3 mm, vias 2 -> 0
- net Net-(U4-RBIAS): track 3.58 -> 8.74 mm
- net /USB_A_DM: track 24.8 -> 19.9 mm
- net PHY_MDC: track 36.7 -> 32.2 mm
- net /USB_A_DP: track 21.3 -> 16.7 mm
- net D-: track 13.3 -> 17.9 mm, vias 0 -> 2
- net Net-(J3-CC1): track 3.24 -> 0.00 mm
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
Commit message: Updated
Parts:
- added C32: 10uF, Capacitor_SMD:C_0603_1608Metric, F.Cu at (128.4, 57.3)
- added C33: 0.1uF, Capacitor_SMD:C_0603_1608Metric, F.Cu at (128.4, 58.8)
- added C34: 10uF, Capacitor_SMD:C_0603_1608Metric, F.Cu at (99.3, 59.0)
- added C35: 0.1uF, Capacitor_SMD:C_0603_1608Metric, F.Cu at (99.3, 60.5)
- added C36: 12pF, Capacitor_SMD:C_0603_1608Metric, F.Cu at (88.0, 64.3)
- added C37: 12pF, Capacitor_SMD:C_0603_1608Metric, F.Cu at (88.8, 61.2)
- added C38: 12pF, Capacitor_SMD:C_0603_1608Metric, F.Cu at (86.6, 68.7)
- added C39: 12pF, Capacitor_SMD:C_0603_1608Metric, F.Cu at (76.8, 67.0)
- C20, C21, C23, R24, R26, R27: moved to B.Cu
- moved R26 11.5 mm to (75.1, 48.6), turned to 180 degrees
- moved R27 9.23 mm to (78.2, 48.6), turned to 0 degrees
- moved R17 7.79 mm to (112.1, 71.2), turned to 180 degrees
- moved R7 6.94 mm to (122.8, 64.8), turned to 180 degrees
- moved C1 6.21 mm to (116.9, 57.9), turned to 90 degrees
- moved D3 6.21 mm to (114.5, 62.3), turned to 0 degrees
- moved R24 5.86 mm to (96.5, 83.9), turned to 0 degrees
- moved R6 5.77 mm to (119.7, 64.8), turned to 0 degrees
- moved C2 4.52 mm to (114.6, 60.4), turned to 180 degrees
- moved D1 4.23 mm to (110.5, 60.9), turned to 180 degrees
- moved C23 4.07 mm to (95.7, 86.3), turned to 90 degrees
- moved D2 4.00 mm to (107.5, 63.6), turned to 0 degrees
- moved R8 3.74 mm to (121.0, 63.2)
- moved R19 3.73 mm to (108.2, 71.2)
- moved C16 3.43 mm to (129.1, 65.9), turned to 90 degrees
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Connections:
- net /USB_A_DM renamed /USB_A_N
- net /USB_A_DP renamed /USB_A_P
- net /USB_C_DM renamed /USB_C_N
- net /USB_C_DP renamed /USB_C_P
- net RD+ renamed ETH_RD+
- net RD- renamed ETH_RD-
- net TD+ renamed ETH_TD+
- net TD- renamed ETH_TD-
- net USB_DM renamed USBHS_N
- net USB_DP renamed USBHS_P
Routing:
- net +5V: track 169.5 -> 318.5 mm, vias 2 -> 6
- net PHY_LED1: track 8.12 -> 69.7 mm
- net PHY_LED2: track 6.42 -> 61.2 mm, vias 0 -> 1
- net ETH_RD+: track 0.00 -> 54.2 mm
- net ETH_RD-: track 0.00 -> 53.9 mm
- net /power_system/Vcc: track 50.3 -> 0.00 mm
- net ETH_TD-: track 0.00 -> 43.6 mm
- net ETH_TD+: track 0.00 -> 43.3 mm
- net GND: track 10.6 -> 35.2 mm, vias 92 -> 355
- net USBHS_P: track 0.00 -> 13.9 mm
- net BOOT: track 0.00 -> 12.7 mm
- net Net-(U4-RBIAS): track 8.74 -> 2.46 mm, vias 0 -> 1
- net /USB_C_N: track 7.51 -> 12.5 mm
- net GNDREF: track 65.2 -> 69.6 mm
- net /USB_C_P: track 8.95 -> 12.1 mm
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- added copper zone on B.Cu, net GND
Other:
- board size 85.2 x 83.8 mm -> 85.4 x 83.8 mm
